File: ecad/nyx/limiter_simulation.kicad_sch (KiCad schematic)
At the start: 7 parts, among them Q1 PMOS, Q2 MMBTA56

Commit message: [WIP] Nyx
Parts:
- added Q3: NMOS, symbol Simulation_SPICE:NMOS
- added V2: ${SIM.PARAMS}, symbol Simulation_SPICE:VDC
- Q1: value PMOS -> RD03P01BAT
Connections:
- net GND: now also Q3.3 (S), V2.2; no longer R2.2
- new net: Q3.1 (D), R2.2
- new net: Q3.2 (G), V2.1

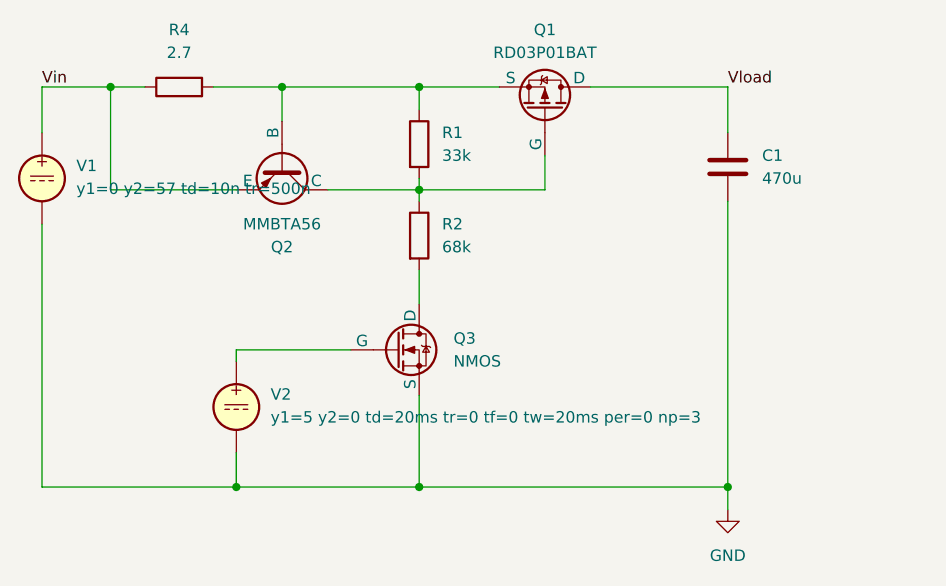
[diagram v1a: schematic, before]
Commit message: [WIP] Building Nyx module
Discovered that a buck-boost inverted controller will be too much (double the VIN). Back to a buck using the hold TPS chip
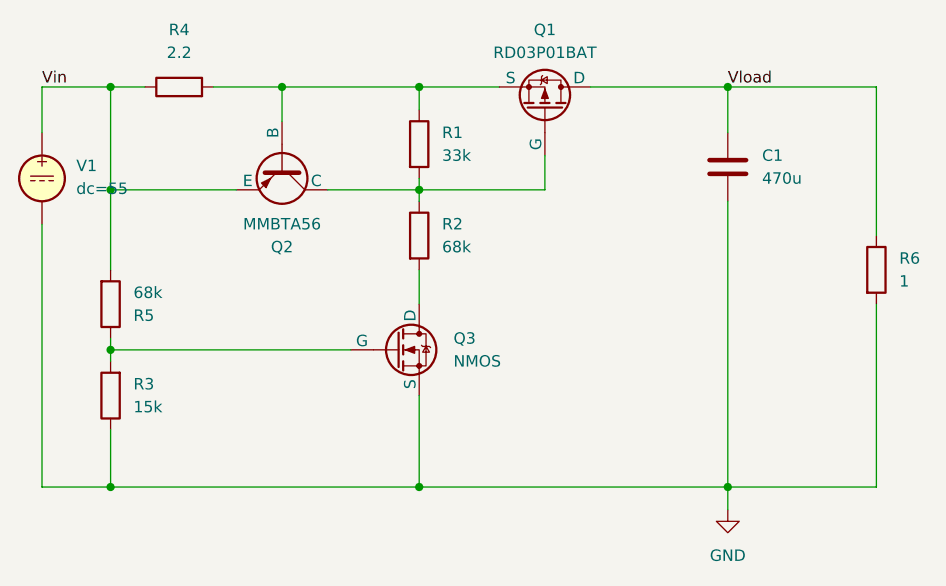
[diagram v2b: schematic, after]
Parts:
- removed V2: ${SIM.PARAMS}, symbol Simulation_SPICE:VDC
- added R3: 15k, symbol Device:R
- added R5: 68k, symbol Device:R
- added R6: 1, symbol Device:R
- R4: value 2.7 -> 2.2
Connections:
- net GND: now also R3.1, R6.2
- net Vin: now also R5.2
- net Vload: now also R6.1
- net at Q3.2 (G): now also R3.2, R5.1

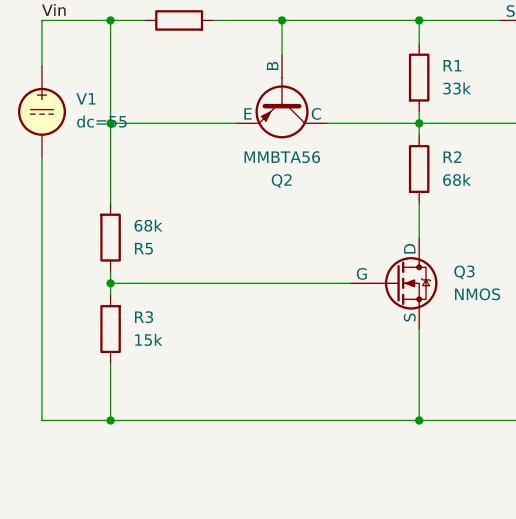
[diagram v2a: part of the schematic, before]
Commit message: Updates Nyx to use only PoRS485
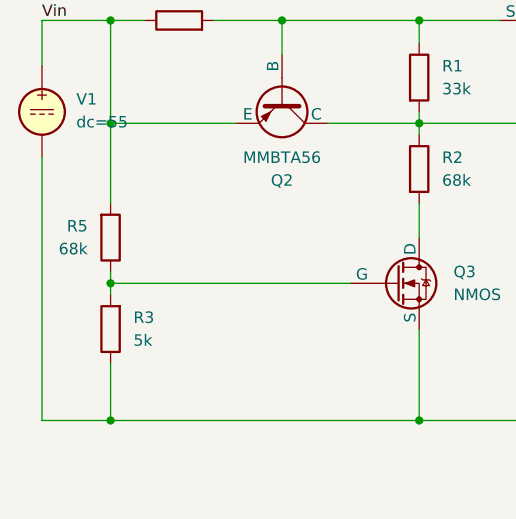
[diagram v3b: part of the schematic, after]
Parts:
- R3: value 15k -> 5k
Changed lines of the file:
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@@
 		(fields_autoplaced yes)
 		(property "Reference" "R5"
-			(at 73.66 88.9001 0)
-			(effects
-				(font
-					(size 1.27 1.27)
-				)
-				(justify left)
+			(at 68.58 86.3599 0)
+			(effects
+				(font
+					(size 1.27 1.27)
+				)
+				(justify right)
 			)
 		)
 		(property "Value" "68k"
-			(at 73.66 86.3601 0)
-			(effects
-				(font
-					(size 1.27 1.27)
-				)
-				(justify left)
+			(at 68.58 88.8999 0)
+			(effects
+				(font
+					(size 1.27 1.27)
+				)
+				(justify right)
 			)
 		)
@@
 			)
 		)
-		(property "Value" "15k"
+		(property "Value" "5k"
 			(at 73.66 99.0599 0)
 			(effects

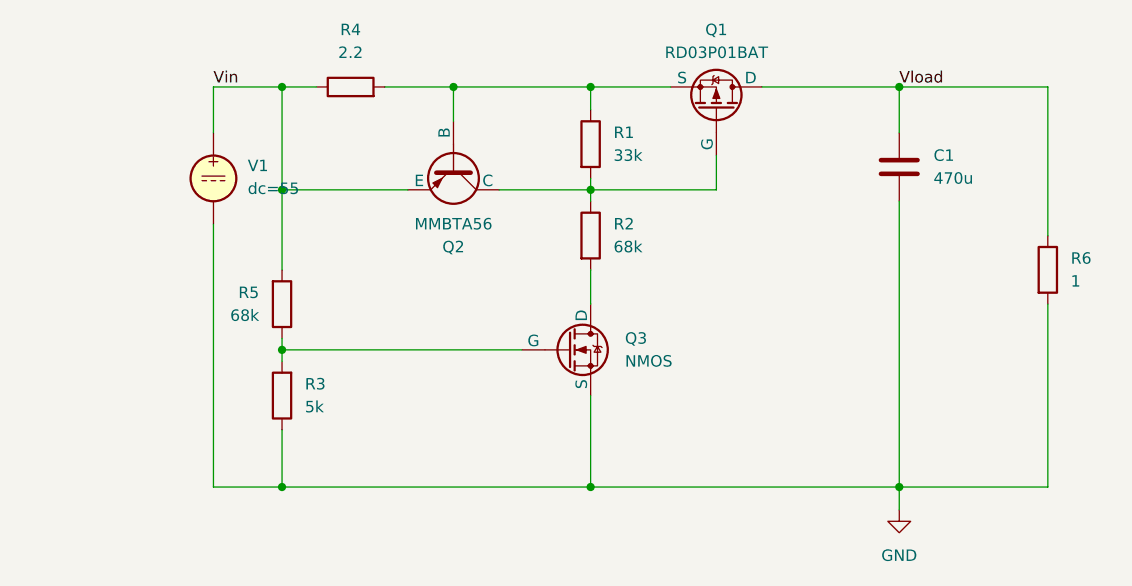
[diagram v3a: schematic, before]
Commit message: Updates Nyx to run on 48V
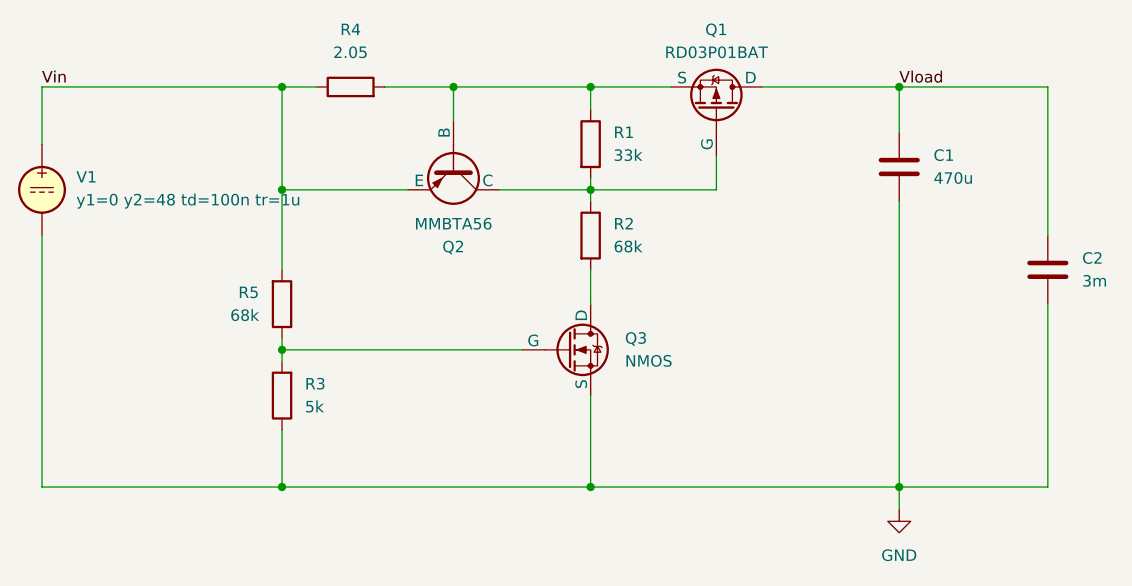
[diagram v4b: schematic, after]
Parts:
- removed R6: 1, symbol Device:R
- added C2: 3m, symbol Device:C
- R4: value 2.2 -> 2.05
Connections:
- net GND: now also C2.2
- net Vload: now also C2.1
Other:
- moved on the sheet: V1
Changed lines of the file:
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@@
 	(wire
 		(pts
-			(xy 63.5 78.74) (xy 63.5 107.95)
+			(xy 44.45 80.01) (xy 44.45 107.95)
 		)
 		(stroke
@@
 	(wire
 		(pts
-			(xy 63.5 68.58) (xy 63.5 63.5)
+			(xy 44.45 69.85) (xy 44.45 63.5)
 		)
 		(stroke
@@
 	(wire
 		(pts
-			(xy 63.5 107.95) (xy 71.12 107.95)
+			(xy 44.45 107.95) (xy 71.12 107.95)
 		)
 		(stroke
@@
 	(wire
 		(pts
-			(xy 63.5 63.5) (xy 71.12 63.5)
+			(xy 44.45 63.5) (xy 71.12 63.5)
 		)
 		(stroke
@@
 	)
 	(label "Vin"
-		(at 63.5 63.5 0)
+		(at 44.45 63.5 0)
 		(fields_autoplaced yes)
 		(effects
@@
 			)
 		)
-		(property "Value" "2.2"
+		(property "Value" "2.05"
 			(at 78.74 59.69 90)
 			(effects
@@
 	(symbol
 		(lib_id "Simulation_SPICE:VDC")
-		(at 63.5 73.66 0)
+		(at 44.45 74.93 0)
 		(unit 1)
 		(exclude_from_sim no)
@@
 		(fields_autoplaced yes)
 		(property "Reference" "V1"
-			(at 67.31 72.2601 0)
+			(at 48.26 73.5301 0)
 			(effects
 				(font
@@
 		)
 		(property "Value" "${SIM.PARAMS}"
-			(at 67.31 74.8001 0)
+			(at 48.26 76.0701 0)
 			(effects
 				(font
@@
 		)
 		(property "Footprint" ""
-			(at 63.5 73.66 0)
+			(at 44.45 74.93 0)
 			(effects
 				(font
@@
 		)
 		(property "Datasheet" "https://ngspice.sourceforge.io/docs/ngspice-html-manual/manual.xhtml#sec_Independent_Sources_for"
-			(at 63.5 73.66 0)
+			(at 44.45 74.93 0)
 			(effects
 				(font
@@
 		)
 		(property "Description" "Voltage source, DC"
-			(at 63.5 73.66 0)
+			(at 44.45 74.93 0)
 			(effects
 				(font
@@
 		)
 		(property "Sim.Pins" "1=+ 2=-"
-			(at 63.5 73.66 0)
-			(effects
-				(font
-					(size 1.27 1.27)
-				)
-				(hide yes)
-			)
-		)
-		(property "Sim.Type" "DC"
-			(at 63.5 73.66 0)
+			(at 44.45 74.93 0)
+			(effects
+				(font
+					(size 1.27 1.27)
+				)
+				(hide yes)
+			)
+		)
+		(property "Sim.Type" "PULSE"
+			(at 44.45 74.93 0)
 			(effects
 				(font
@@
 		)
 		(property "Sim.Device" "V"
-			(at 63.5 73.66 0)
+			(at 44.45 74.93 0)
 			(effects
 				(font
@@
 			)
 		)
-		(property "Sim.Params" "dc=55"
-			(at 63.5 73.66 0)
+		(property "Sim.Params" "y1=0 y2=48 td=100n tr=1u"
+			(at 44.45 74.93 0)
 			(effects
 				(font
@@
 	)
 	(symbol
-		(lib_id "Device:R")
+		(lib_id "Device:C")
 		(at 156.21 83.82 0)
 		(unit 1)
@@
 		(dnp no)
 		(fields_autoplaced yes)
-		(property "Reference" "R6"
-			(at 158.75 82.5499 0)
+		(property "Reference" "C2"
+			(at 160.02 82.5499 0)
 			(effects
 				(font
@@
 			)
 		)
-		(property "Value" "1"
-			(at 158.75 85.0899 0)
+		(property "Value" "3m"
+			(at 160.02 85.0899 0)
 			(effects
 				(font
@@
 		)
 		(property "Footprint" ""
-			(at 154.432 83.82 90)
+			(at 157.1752 87.63 0)
 			(effects
 				(font
@@
 			)
 		)
-		(property "Description" "Resistor"
+		(property "Description" "Unpolarized capacitor"
 			(at 156.21 83.82 0)
 			(effects
@@
 			)
 		)
+		(pin "1"
+		)
 		(pin "2"
-		)
-		(pin "1"
 		)
 		(instances
 			(project "limiter_simulation"
 				(path "/2f730959-4e9b-4d39-82b6-06bb2796907d"
-					(reference "R6")
+					(reference "C2")
 					(unit 1)
 				)

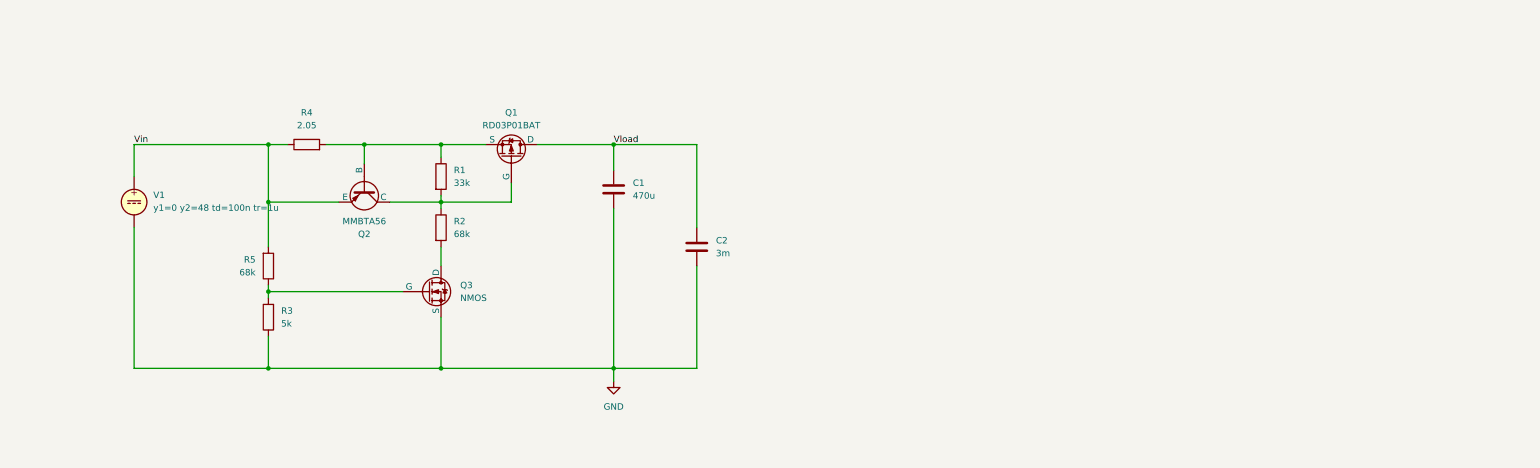
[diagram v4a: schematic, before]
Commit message: Updates nyx to block reverse current
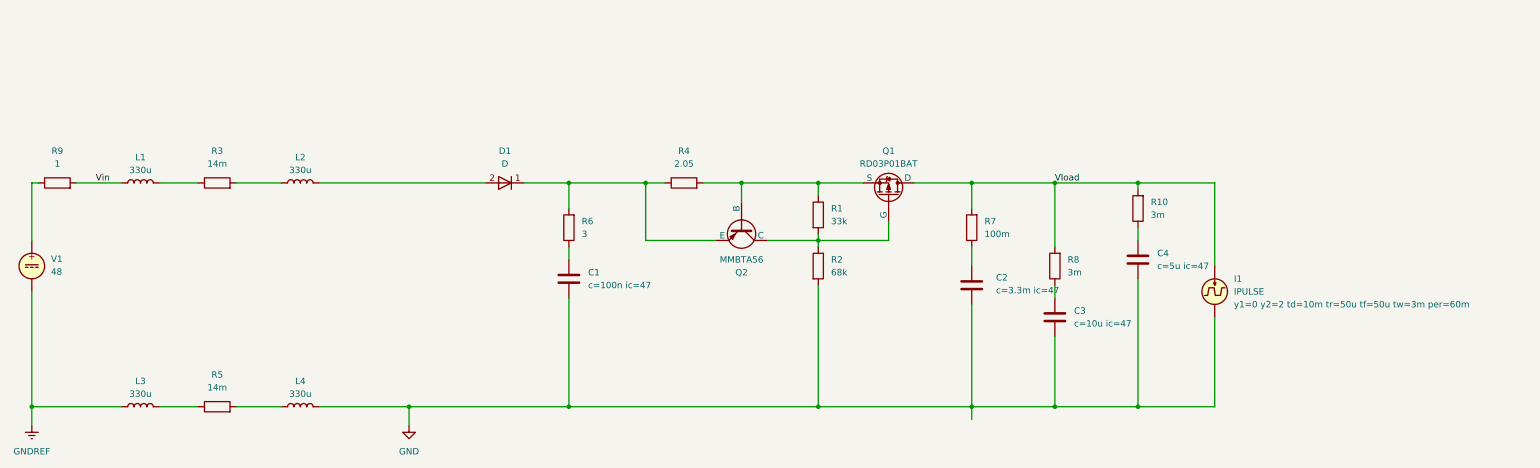
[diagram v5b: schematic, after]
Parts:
- removed Q3: NMOS, symbol Simulation_SPICE:NMOS
- added C3, C4: ${SIM.PARAMS}, symbol Device:C
- added D1: D, symbol Simulation_SPICE:D
- added I1: IPULSE, symbol Simulation_SPICE:IPULSE
- added L1, L2, L3, L4: 330u, symbol Device:L
- added R10, R8: 3m, symbol Device:R
- added R6: 3, symbol Device:R
- added R7: 100m, symbol Device:R
- added R9: 1, symbol Device:R
- C1: value 470u -> ${SIM.PARAMS}
- C2: value 3m -> ${SIM.PARAMS}
- R3: value 5k -> 14m
- R5: value 68k -> 14m
- V1: value ${SIM.PARAMS} -> 48
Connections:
- net GND: now also R2.2, C3.2, C4.2, I1.2, L4.2; no longer R3.1, V1.2
- net Vin: now also L1.1, R9.2; no longer Q2.3 (E), R4.1, R5.2, V1.1
- net Vload: now also I1.1, R10.2, R7.2, R8.2; no longer C1.1, C2.1
- net at R3.2: now also L2.1; no longer R5.1
- new net: D1.2 (A), L2.2
- new net: L3.2, R5.1
- new net: L4.1, R5.2
- new net: D1.1 (K), Q2.3 (E), R4.1, R6.2
- new net: R9.1, V1.1
- new net: C1.1, R6.1
- new net: L1.2, R3.1
- new net: C4.1, R10.1
- new net: C2.1, R7.1
- new net: C3.1, R8.1
- new net GNDREF: L3.1, V1.2
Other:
- moved on the sheet: C2, Q1, Q2, R1, R2, R4

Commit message: Simulate load deconnection.
In short: do not do it.
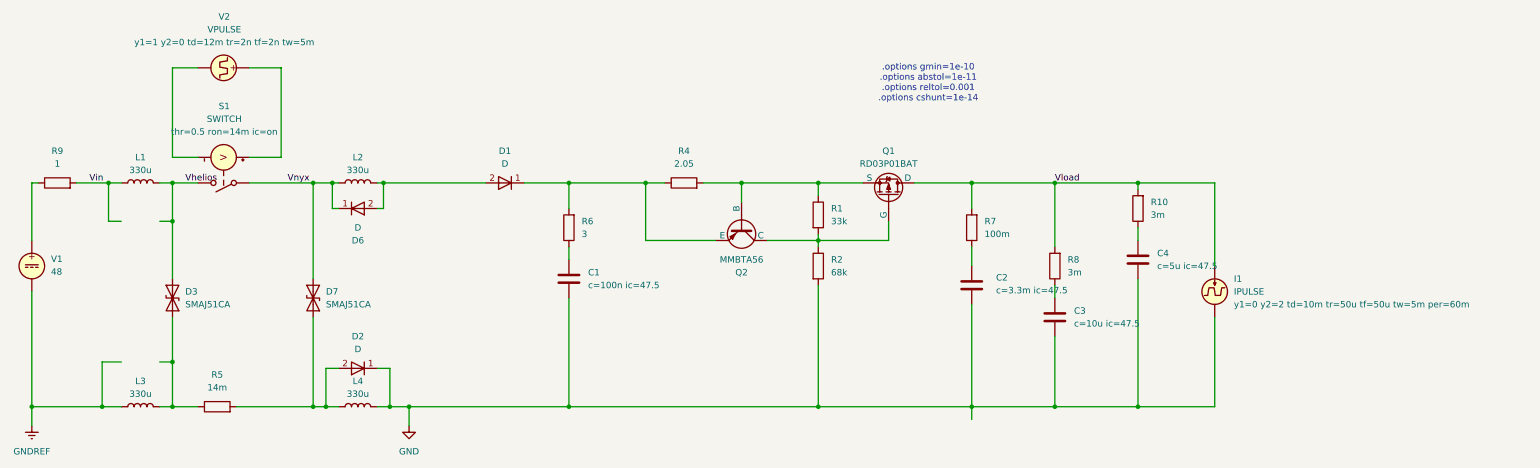
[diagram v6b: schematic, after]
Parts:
- removed R3: 14m, symbol Device:R
- added D2, D6: D, symbol Simulation_SPICE:D
- added D3, D7: SMAJ51CA, Diode_SMD:D_SMA, symbol Diode:SMAJ51CA
- added S1: SWITCH, symbol Simulation_SPICE:SWITCH
- added V2: VPULSE, symbol Simulation_SPICE:VPULSE
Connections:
- net GND: now also D2.1 (K)
- net Vnyx: now reaches L2.1
- net Vnyx: now also D6.1 (K), D7.2 (A2), S1.1 (N+)
- net at D1.2 (A), L2.2: now also D6.2 (A)
- net at L3.2, R5.1: now also D3.1 (A1)
- net at L4.1, R5.2: now also D2.2 (A), D7.1 (A1)
- net Vhelios: now reaches L1.2
- net Vhelios: now also D3.2 (A2), S1.2 (N-)
- new net: S1.3 (C+), V2.1
- new net: S1.4 (C-), V2.2
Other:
- note added: ".options gmin=1e-10 .options abstol=1e-11 .options reltol=0.001 .options cshunt=1e-14"
- moved on the sheet: L2, L4

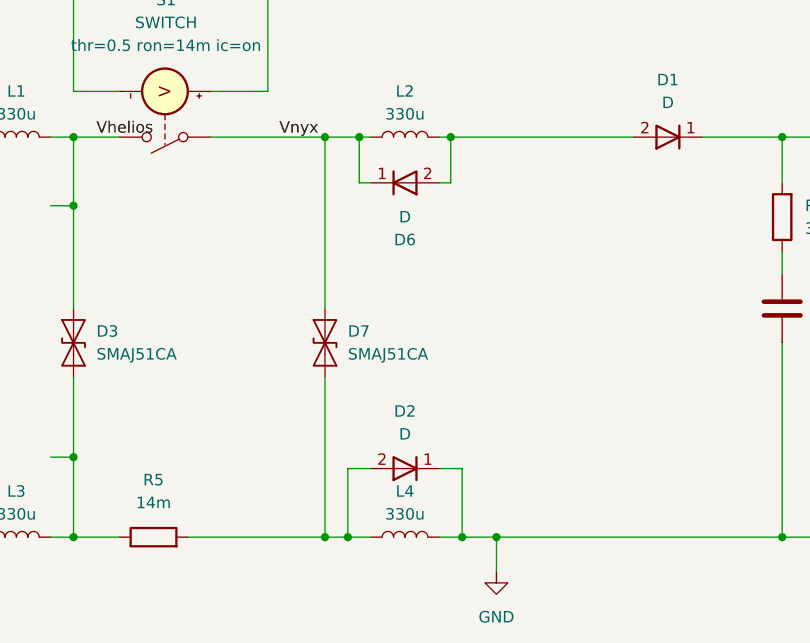
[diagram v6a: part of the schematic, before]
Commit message: Updates MPN for new PCBs
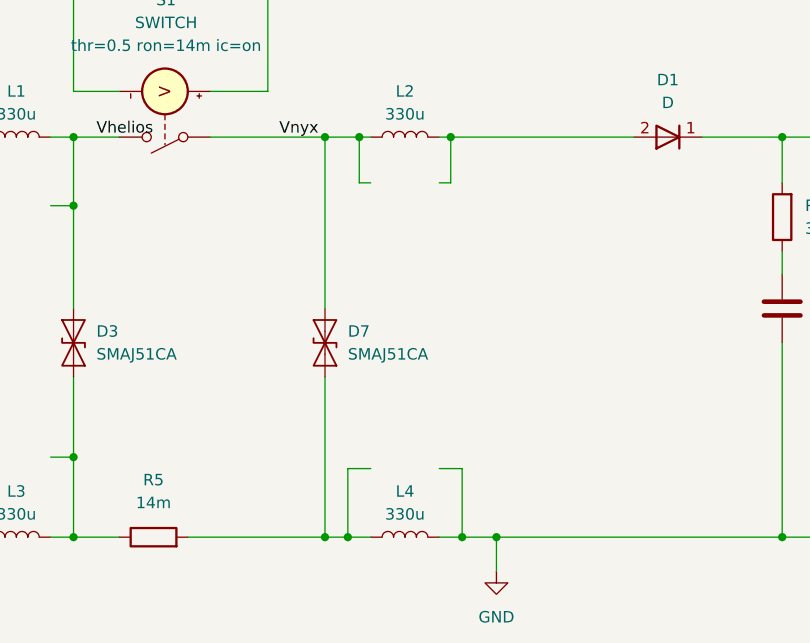
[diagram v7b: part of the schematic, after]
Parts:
- removed D2, D6: D, symbol Simulation_SPICE:D
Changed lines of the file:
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@@
-	)
-	(symbol
-		(lib_id "Simulation_SPICE:D")
-		(at 88.9 107.95 180)
-		(unit 1)
-		(exclude_from_sim no)
-		(in_bom yes)
-		(on_board yes)
-		(dnp no)
-		(fields_autoplaced yes)
-		(property "Reference" "D2"
-			(at 88.9 101.6 0)
-			(effects
-				(font
-					(size 1.27 1.27)
-				)
-			)
-		)
-		(property "Value" "D"
-			(at 88.9 104.14 0)
-			(effects
-				(font
-					(size 1.27 1.27)
-				)
-			)
-		)
-		(property "Footprint" ""
-			(at 88.9 107.95 0)
-			(effects
-				(font
-					(size 1.27 1.27)
-				)
-				(hide yes)
-			)
-		)
-		(property "Datasheet" "https://ngspice.sourceforge.io/docs/ngspice-html-manual/manual.xhtml#cha_DIODEs"
-			(at 88.9 107.95 0)
-			(effects
-				(font
-					(size 1.27 1.27)
-				)
-				(hide yes)
-			)
-		)
-		(property "Description" "Diode for simulation or PCB"
-			(at 88.9 107.95 0)
-			(effects
-				(font
-					(size 1.27 1.27)
-				)
-				(hide yes)
-			)
-		)
-		(property "Sim.Device" "SUBCKT"
-			(at 88.9 107.95 0)
-			(effects
-				(font
-					(size 1.27 1.27)
-				)
-				(hide yes)
-			)
-		)
-		(property "Sim.Pins" "1=2 2=1"
-			(at 88.9 107.95 0)
-			(effects
-				(font
-					(size 1.27 1.27)
-				)
-				(hide yes)
-			)
-		)
-		(property "Sim.Library" "lib/PMEG6030EVP.lib"
-			(at 88.9 107.95 0)
-			(effects
-				(font
-					(size 1.27 1.27)
-				)
-				(hide yes)
-			)
-		)
-		(property "Sim.Name" "PMEG6030EVP"
-			(at 88.9 107.95 0)
-			(effects
-				(font
-					(size 1.27 1.27)
-				)
-				(hide yes)
-			)
-		)
-		(pin "1"
-		)
-		(pin "2"
-		)
-		(instances
-			(project "limiter_simulation"
-				(path "/2f730959-4e9b-4d39-82b6-06bb2796907d"
-					(reference "D2")
-					(unit 1)
-				)
-			)
-		)
 	)
 	(symbol
@@
 					(unit 1)
 				)
-			)
-		)
-	)
-	(symbol
-		(lib_id "Simulation_SPICE:D")
-		(at 88.9 76.2 0)
-		(mirror x)
-		(unit 1)
-		(exclude_from_sim no)
-		(in_bom yes)
-		(on_board yes)
-		(dnp no)
-		(property "Reference" "D6"
-			(at 88.9 82.55 0)
-			(effects
-				(font
-					(size 1.27 1.27)
-				)
-			)
-		)
-		(property "Value" "D"
-			(at 88.9 80.01 0)
-			(effects
-				(font
-					(size 1.27 1.27)
-				)
-			)
-		)
-		(property "Footprint" ""
-			(at 88.9 76.2 0)
-			(effects
-				(font
-					(size 1.27 1.27)
-				)
-				(hide yes)
-			)
-		)
-		(property "Datasheet" "https://ngspice.sourceforge.io/docs/ngspice-html-manual/manual.xhtml#cha_DIODEs"
-			(at 88.9 76.2 0)
-			(effects
-				(font
-					(size 1.27 1.27)
-				)
-				(hide yes)
-			)
-		)
-		(property "Description" "Diode for simulation or PCB"
-			(at 88.9 76.2 0)
-			(effects
-				(font
-					(size 1.27 1.27)
-				)
-				(hide yes)
-			)
-		)
-		(property "Sim.Device" "SUBCKT"
-			(at 88.9 76.2 0)
-			(effects
-				(font
-					(size 1.27 1.27)
-				)
-				(hide yes)
-			)
-		)
-		(property "Sim.Pins" "1=2 2=1"
-			(at 88.9 76.2 0)
-			(effects
-				(font
-					(size 1.27 1.27)
-				)
-				(hide yes)
-			)
-		)
-		(property "Sim.Library" "lib/PMEG6030EVP.lib"
-			(at 88.9 76.2 0)
-			(effects
-				(font
-					(size 1.27 1.27)
-				)
-				(hide yes)
-			)
-		)
-		(property "Sim.Name" "PMEG6030EVP"
-			(at 88.9 76.2 0)
-			(effects
-				(font
-					(size 1.27 1.27)
-				)
-				(hide yes)
-			)
-		)
-		(pin "1"
-		)
-		(pin "2"
-		)
-		(instances
-			(project "limiter_simulation"
-				(path "/2f730959-4e9b-4d39-82b6-06bb2796907d"
-					(reference "D6")
-					(unit 1)
-				)
